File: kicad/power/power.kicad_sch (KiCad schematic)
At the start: 20 parts, among them J1 Conn_01x05, K1 SRD-12VDC-SL-C, P1 CONN_2, P2 CONN_3, P3 CONN_2, P4 CONN_2

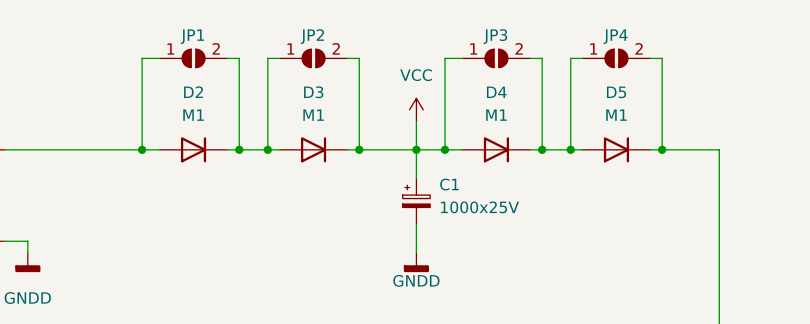
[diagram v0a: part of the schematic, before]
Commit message: На питании диоды замкнул перемычками
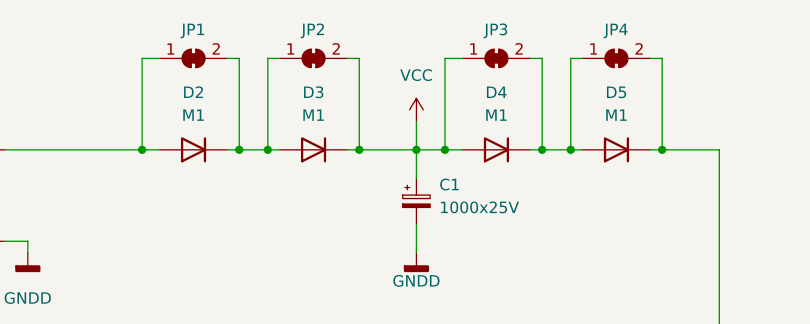
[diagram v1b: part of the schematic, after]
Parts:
- removed JP1, JP2, JP3, JP4: SolderJumper_2_Open, Jumper:SolderJumper-2_P1.3mm_Open_RoundedPad1.0x1.5mm, symbol Jumper:SolderJumper_2_Open
- added JP1, JP2, JP3, JP4: SolderJumper_2_Bridged, Jumper:SolderJumper-2_P1.3mm_Bridged_Pad1.0x1.5mm, symbol Jumper:SolderJumper_2_Bridged
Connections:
- net VCC: now also JP2.2 (B), JP3.1 (A)
- net at BD1.1 (+), D2.2 (A): now also JP1.1 (A)
- net at D2.1 (K), D3.2 (A): now also JP1.2 (B), JP2.1 (A)
- net at D5.1 (K), J1.1 (Pin_1): now also JP4.2 (B)
- net at D4.1 (K), D5.2 (A): now also JP3.2 (B), JP4.1 (A)
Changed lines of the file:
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@@
     (pin "2")
   )
-  (symbol (lib_id "Jumper:SolderJumper_2_Open") (at 180.975 39.37 0) (unit 1)
-    (in_bom yes) (on_board yes)
-    (property "Reference" "JP4" (id 0) (at 180.975 36.83 0))
-    (property "Value" "SolderJumper_2_Open" (id 1) (at 180.975 36.195 0)
-      (effects (font (size 1.27 1.27)) hide)
-    )
-    (property "Footprint" "Jumper:SolderJumper-2_P1.3mm_Open_RoundedPad1.0x1.5mm" (id 2) (at 180.975 39.37 0)
-      (effects (font (size 1.27 1.27)) hide)
-    )
-    (property "Datasheet" "~" (id 3) (at 180.975 39.37 0)
+  (symbol (lib_id "Jumper:SolderJumper_2_Bridged") (at 167.64 39.37 0) (unit 1)
+    (in_bom yes) (on_board yes)
+    (property "Reference" "JP3" (id 0) (at 167.64 36.195 0))
+    (property "Value" "SolderJumper_2_Bridged" (id 1) (at 167.64 36.195 0)
+      (effects (font (size 1.27 1.27)) hide)
+    )
+    (property "Footprint" "Jumper:SolderJumper-2_P1.3mm_Bridged_Pad1.0x1.5mm" (id 2) (at 167.64 39.37 0)
+      (effects (font (size 1.27 1.27)) hide)
+    )
+    (property "Datasheet" "~" (id 3) (at 167.64 39.37 0)
       (effects (font (size 1.27 1.27)) hide)
     )
@@
     (property "Datasheet" "" (id 3) (at 59.055 54.61 0)
       (effects (font (size 1.524 1.524)))
-    )
-    (pin "1")
-    (pin "2")
-  )
-  (symbol (lib_id "Jumper:SolderJumper_2_Open") (at 167.64 39.37 0) (unit 1)
-    (in_bom yes) (on_board yes)
-    (property "Reference" "JP3" (id 0) (at 167.64 36.83 0))
-    (property "Value" "SolderJumper_2_Open" (id 1) (at 167.64 36.195 0)
-      (effects (font (size 1.27 1.27)) hide)
-    )
-    (property "Footprint" "Jumper:SolderJumper-2_P1.3mm_Open_RoundedPad1.0x1.5mm" (id 2) (at 167.64 39.37 0)
-      (effects (font (size 1.27 1.27)) hide)
-    )
-    (property "Datasheet" "~" (id 3) (at 167.64 39.37 0)
-      (effects (font (size 1.27 1.27)) hide)
     )
     (pin "1")
@@
     (pin "5")
   )
+  (symbol (lib_id "Jumper:SolderJumper_2_Bridged") (at 147.32 39.37 0) (unit 1)
+    (in_bom yes) (on_board yes)
+    (property "Reference" "JP2" (id 0) (at 147.32 36.195 0))
+    (property "Value" "SolderJumper_2_Bridged" (id 1) (at 147.32 36.195 0)
+      (effects (font (size 1.27 1.27)) hide)
+    )
+    (property "Footprint" "Jumper:SolderJumper-2_P1.3mm_Bridged_Pad1.0x1.5mm" (id 2) (at 147.32 39.37 0)
+      (effects (font (size 1.27 1.27)) hide)
+    )
+    (property "Datasheet" "~" (id 3) (at 147.32 39.37 0)
+      (effects (font (size 1.27 1.27)) hide)
+    )
+    (pin "1")
+    (pin "2")
+  )
   (symbol (lib_id "разъемы:CONN_2") (at 207.01 117.475 0) (unit 1)
     (in_bom yes) (on_board yes) (fields_autoplaced)
@@
     (pin "2")
   )
+  (symbol (lib_id "Jumper:SolderJumper_2_Bridged") (at 133.985 39.37 0) (unit 1)
+    (in_bom yes) (on_board yes)
+    (property "Reference" "JP1" (id 0) (at 133.985 36.195 0))
+    (property "Value" "SolderJumper_2_Bridged" (id 1) (at 133.985 36.195 0)
+      (effects (font (size 1.27 1.27)) hide)
+    )
+    (property "Footprint" "Jumper:SolderJumper-2_P1.3mm_Bridged_Pad1.0x1.5mm" (id 2) (at 133.985 39.37 0)
+      (effects (font (size 1.27 1.27)) hide)
+    )
+    (property "Datasheet" "~" (id 3) (at 133.985 39.37 0)
+      (effects (font (size 1.27 1.27)) hide)
+    )
+    (pin "1")
+    (pin "2")
+  )
   (symbol (lib_id "power:GNDD") (at 199.39 80.645 0) (unit 1)
     (in_bom yes) (on_board yes) (fields_autoplaced)
@@
     )
     (pin "1")
-  )
-  (symbol (lib_id "Jumper:SolderJumper_2_Open") (at 147.32 39.37 0) (unit 1)
-    (in_bom yes) (on_board yes)
-    (property "Reference" "JP2" (id 0) (at 147.32 36.83 0))
-    (property "Value" "SolderJumper_2_Open" (id 1) (at 147.32 36.195 0)
-      (effects (font (size 1.27 1.27)) hide)
-    )
-    (property "Footprint" "Jumper:SolderJumper-2_P1.3mm_Open_RoundedPad1.0x1.5mm" (id 2) (at 147.32 39.37 0)
-      (effects (font (size 1.27 1.27)) hide)
-    )
-    (property "Datasheet" "~" (id 3) (at 147.32 39.37 0)
-      (effects (font (size 1.27 1.27)) hide)
-    )
-    (pin "1")
-    (pin "2")
   )
   (symbol (lib_id "Transformer:TEZ2.0-D-1") (at 81.28 54.61 0) (unit 1)
@@
     (pin "9")
   )
+  (symbol (lib_id "Jumper:SolderJumper_2_Bridged") (at 180.975 39.37 0) (unit 1)
+    (in_bom yes) (on_board yes)
+    (property "Reference" "JP4" (id 0) (at 180.975 36.195 0))
+    (property "Value" "SolderJumper_2_Bridged" (id 1) (at 180.975 36.195 0)
+      (effects (font (size 1.27 1.27)) hide)
+    )
+    (property "Footprint" "Jumper:SolderJumper-2_P1.3mm_Bridged_Pad1.0x1.5mm" (id 2) (at 180.975 39.37 0)
+      (effects (font (size 1.27 1.27)) hide)
+    )
+    (property "Datasheet" "~" (id 3) (at 180.975 39.37 0)
+      (effects (font (size 1.27 1.27)) hide)
+    )
+    (pin "1")
+    (pin "2")
+  )
   (symbol (lib_id "реле:Реле_2-3") (at 96.52 107.315 0) (mirror y) (unit 1)
     (in_bom yes) (on_board yes)
@@
     (pin "5")
   )
-  (symbol (lib_id "Jumper:SolderJumper_2_Open") (at 133.985 39.37 0) (unit 1)
-    (in_bom yes) (on_board yes)
-    (property "Reference" "JP1" (id 0) (at 133.985 36.83 0))
-    (property "Value" "SolderJumper_2_Open" (id 1) (at 133.985 36.195 0)
-      (effects (font (size 1.27 1.27)) hide)
-    )
-    (property "Footprint" "Jumper:SolderJumper-2_P1.3mm_Open_RoundedPad1.0x1.5mm" (id 2) (at 133.985 39.37 0)
-      (effects (font (size 1.27 1.27)) hide)
-    )
-    (property "Datasheet" "~" (id 3) (at 133.985 39.37 0)
-      (effects (font (size 1.27 1.27)) hide)
-    )
-    (pin "1")
-    (pin "2")
-  )
   (sheet_instances
     (path "/" (page "1"))
@@
       (reference "J1") (unit 1) (value "Conn_01x05") (footprint "Connector_JST:JST_EH_B5B-EH-A_1x05_P2.50mm_Vertical")
     )
-    (path "/f892873a-cc0c-4508-a181-3989549c054b"
-      (reference "JP1") (unit 1) (value "SolderJumper_2_Open") (footprint "Jumper:SolderJumper-2_P1.3mm_Open_RoundedPad1.0x1.5mm")
-    )
-    (path "/c9023247-54ce-4c0a-9ed3-6ca9e3d6e2db"
-      (reference "JP2") (unit 1) (value "SolderJumper_2_Open") (footprint "Jumper:SolderJumper-2_P1.3mm_Open_RoundedPad1.0x1.5mm")
-    )
-    (path "/9e769c63-3ae3-4dda-8be9-5f691d16c9f3"
-      (reference "JP3") (unit 1) (value "SolderJumper_2_Open") (footprint "Jumper:SolderJumper-2_P1.3mm_Open_RoundedPad1.0x1.5mm")
-    )
-    (path "/84b85db5-0987-461e-a2b0-6609fd9db402"
-      (reference "JP4") (unit 1) (value "SolderJumper_2_Open") (footprint "Jumper:SolderJumper-2_P1.3mm_Open_RoundedPad1.0x1.5mm")
+    (path "/b7b90600-6df0-4c2c-9254-df3c0c605432"
+      (reference "JP1") (unit 1) (value "SolderJumper_2_Bridged") (footprint "Jumper:SolderJumper-2_P1.3mm_Bridged_Pad1.0x1.5mm")
+    )
+    (path "/af17939f-543d-4271-b959-061a19aa2c0f"
+      (reference "JP2") (unit 1) (value "SolderJumper_2_Bridged") (footprint "Jumper:SolderJumper-2_P1.3mm_Bridged_Pad1.0x1.5mm")
+    )
+    (path "/7ec32a02-f6a8-4cb9-8e19-68118e2b04fd"
+      (reference "JP3") (unit 1) (value "SolderJumper_2_Bridged") (footprint "Jumper:SolderJumper-2_P1.3mm_Bridged_Pad1.0x1.5mm")
+    )
+    (path "/f0c7a894-7a84-4b20-a3f2-a41d9b7fb398"
+      (reference "JP4") (unit 1) (value "SolderJumper_2_Bridged") (footprint "Jumper:SolderJumper-2_P1.3mm_Bridged_Pad1.0x1.5mm")
     )
     (path "/f3258521-27ee-49b2-b6fc-104e5de7fa29"

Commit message: Детали, стоимость
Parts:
- BD1: Aliexpress (none) -> https://aliexpress.ru/item/1005002106188652.html?sku_id=120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; ChipDip (none) -> https://www.chipdip.ru/product/mb10f-hottech; Цена2 (none) -> =200/50
- C1: ChipDip (none) -> https://www.chipdip.ru/product0/9000565924
- D1, D2, D3, D4, D5: Aliexpress (none) -> https://aliexpress.ru/item/4000331358747.html?sku_id=100000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; ChipDip (none) -> https://www.chipdip.ru/product/m1-sunmate; Цена2 (none) -> =90/100
- J1: Aliexpress (none) -> https://aliexpress.ru/item/32701800317.html?spm=a2g2w.store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; ChipDip (none) -> https://aliexpress.ru/item/32701800317.html?spm=a2g2w.store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; Цена 2,6 -> =160/50; Цена2 (none) -> =160/50
- JP1, JP2, JP3, JP4: Цена (none) -> 0; Цена2 (none) -> 0
- K1: Aliexpress (none) -> https://aliexpress.ru/item/1005001994042589.html?sku_id=120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; ChipDip (none) -> https://www.chipdip.ru/product0/8023333076; Цена 37 -> 60; Цена2 (none) -> 37
- P1: Aliexpress (none) -> https://aliexpress.ru/item/32979388954.html?sku_id=66712511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; ChipDip (none) -> https://www.chipdip.ru/product/dg500-5.08-02p-14-00ah; Цена (none) -> 38; Цена2 (none) -> =133/10
- P2: Aliexpress (none) -> https://aliexpress.ru/item/32979388954.html?sku_id=66712511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; ChipDip (none) -> https://www.chipdip.ru/product/dg500-5.08-03p-14-00a-h; Цена 14,1 -> 42; Цена2 (none) -> =146/10
- P3, P4: Aliexpress (none) -> https://aliexpress.ru/item/32979388954.html?sku_id=66712511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; ChipDip (none) -> https://www.chipdip.ru/product/dg500-5.08-02p-14-00ah; Цена 12,7 -> 38; Цена2 (none) -> =133/10
- TR1: Aliexpress (none) -> https://www.chipdip.ru/product0/8010765633; ChipDip (none) -> https://www.chipdip.ru/product/tpk-1-9v; ChipDip2 https://www.chipdip.ru/product0/8010765633 -> (none); Цена2 2*320 -> =320
